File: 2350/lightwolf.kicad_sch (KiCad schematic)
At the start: 52 parts, among them Q1 XC6220B331MR-G, U1 DS1021-1X20SF11-B, U2 W25Q32JVSNIQ, U3 DS1021-1X20SF11-B, U4 RP2350A_C42411118, U5 ABM8-272-T3_C20625731, U6 0603L100SLYR

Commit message: feat: update design files and add production files
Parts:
- C12: renamed from C3; value 4.7uF -> 10uF; symbol PCM_JLCPCB-Capacitors:0402,4.7uF -> PCM_JLCPCB-Capacitors:0402,10uF; Capacitance 4.7uF -> 10uF; LCSC C23733 -> C15525; Part CL05A475MP5NRNC -> CL05A106MQ5NUNC; Price 0.008USD -> 0.009USD; Stock 3319340 -> 3940889; Voltage Rated 10V -> 6.3V
- renumbered C4 to C1, C19 to C10, C20 to C11, C9 to C13, C12 to C14, C14 to C15, C2 to C16, C5 to C17, C11 to C18, C7 to C19, C6 to C2, C8 to C3, C10 to C4, C13 to C5, C15 to C6, C16 to C7, C17 to C8, C1 to C9, H3 to H2, H2 to H3, R8 to R1, R11 to R10, R12 to R11, R13 to R12, R4 to R13, R10 to R4, R9 to R5, R5 to R6, R6 to R7, R1 to R8, R7 to R9, U5 to U1, U6 to U2, U2 to U3, U1 to U5, U3 to U6

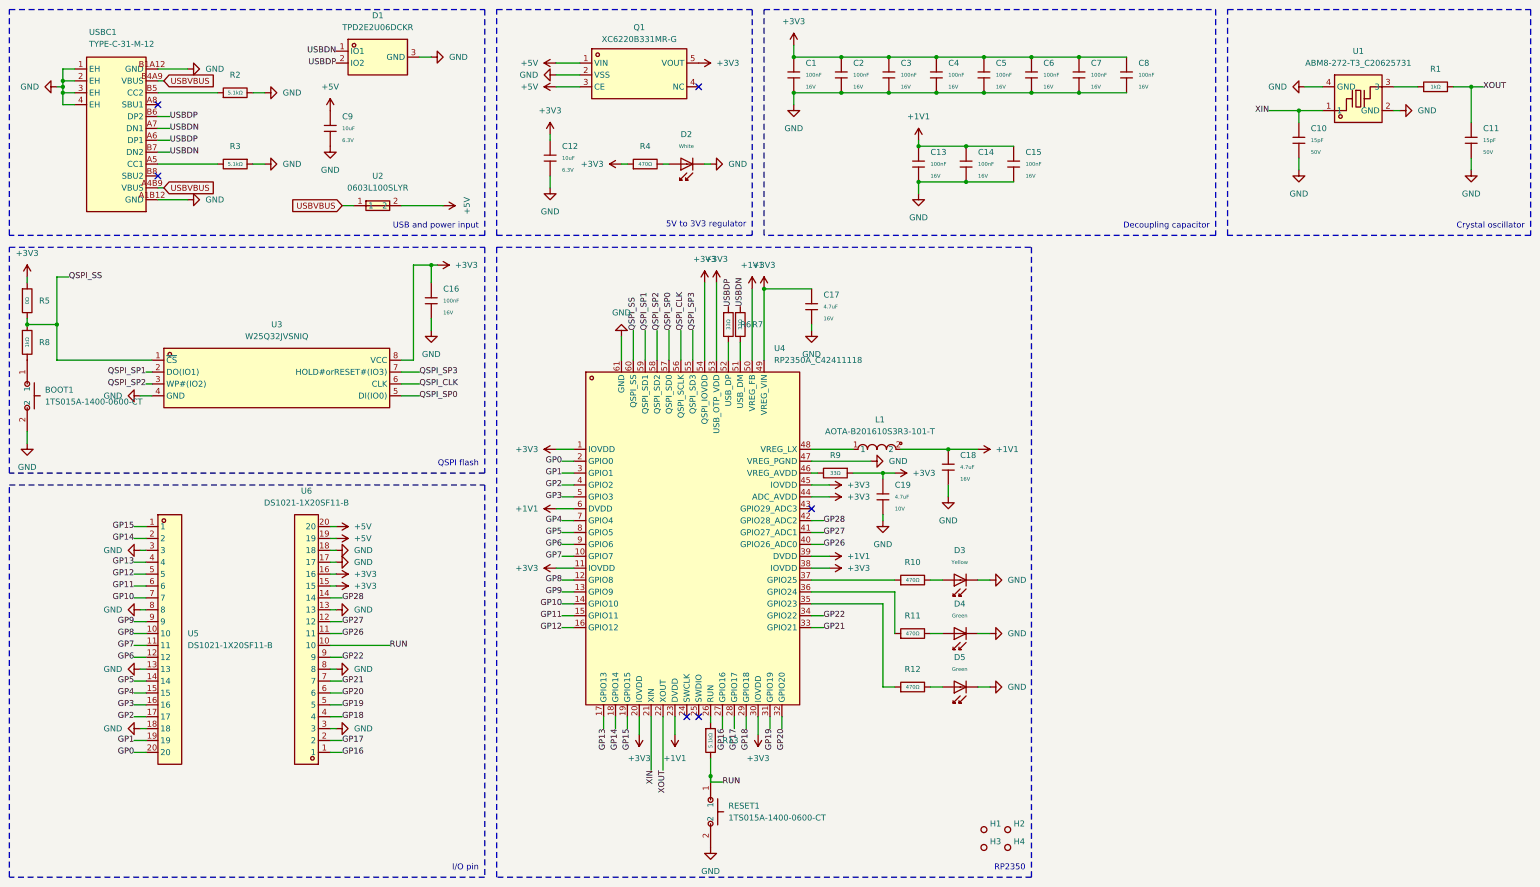
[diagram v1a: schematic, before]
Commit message: fix: design issue and update project files
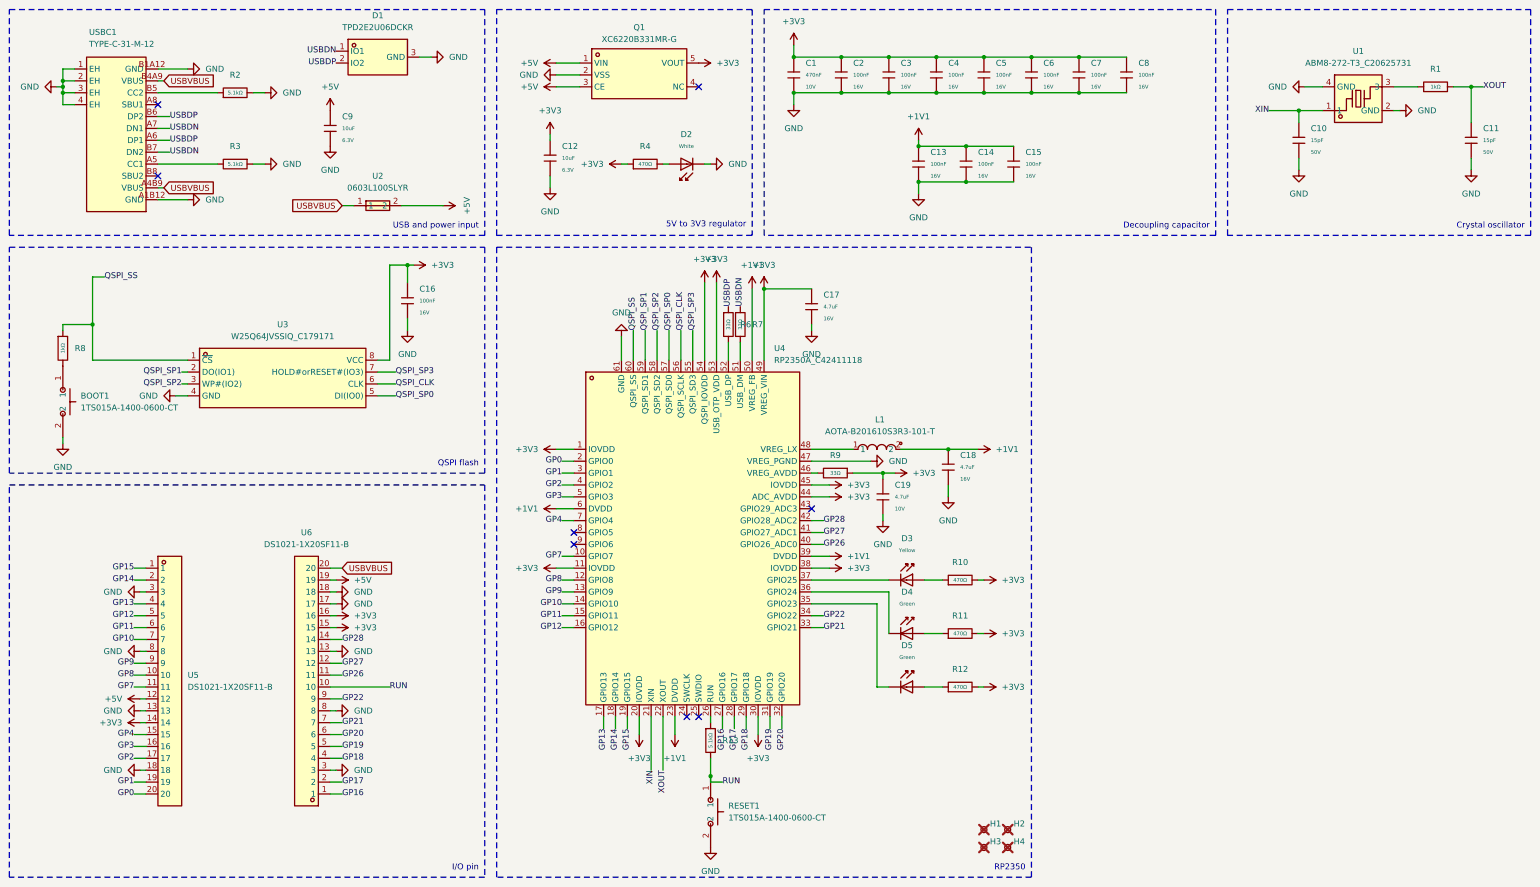
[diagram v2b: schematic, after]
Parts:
- removed D2: White, PCM_JLCPCB:D_0805, symbol PCM_JLCPCB-Diodes:LED,0805,White
- removed R5: 0Ω, PCM_JLCPCB:R_0402, symbol PCM_JLCPCB-Resistors:0402,0Ω
- added D2: White, PCM_JLCPCB:D_0603, symbol PCM_JLCPCB-Diodes:LED,0603,White
- C1: value 100nF -> 470nF; symbol PCM_JLCPCB-Capacitors:0402,100nF -> PCM_JLCPCB-Capacitors:0402,470nF; Attrition Qty 10 -> 12; Capacitance 100nF -> 470nF; Class Basic Component -> Preferred Component; LCSC C1525 -> C47339; Part CL05B104KO5NNNC -> CL05A474KP5NNNC; Price 0.004USD -> 0.007USD; Stock 14407666 -> 84633; Temperature Coefficient X7R -> X5R; Voltage Rated 16V -> 10V
- H1, H2, H3, H4: now not fitted; now left out of the parts list
- U3: value W25Q32JVSNIQ -> W25Q64JVSSIQ_C179171; footprint easyeda2kicad:SOP-8_L4.9-W3.9-P1.27-LS6.0-BL -> easyeda2kicad:SOIC-8_L5.3-W5.3-P1.27-LS8.0-BL; symbol easyeda2kicad:W25Q32JVSNIQ -> easyeda2kicad:W25Q64JVSSIQ_C179171; LCSC Part C5355146 -> C179171
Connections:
- net +3V3: now also R10.2, R11.2, R12.2, U5.14
- net +5V: now also U5.12; no longer U6.20
- net GND: now also D2.1; no longer D3.1, D4.1, D5.1
- net USBVBUS: now also U6.20
- net at R11.1: now also D4.2; no longer U4.36 (GPIO24)
- net at R12.1: now also D5.2; no longer U4.35 (GPIO23)
- net at U4.37 (GPIO25): now also D3.1; no longer R10.1
- net at D3.2: now also R10.1; no longer R10.2
- net at R4.2: now also D2.2
- net GP5: no longer names the net of U4.8 (GPIO5)
- net GP5: no longer U5.14
- net GP6: no longer names the net of U4.9 (GPIO6)
- net GP6: no longer U5.12
- new net: D5.1, U4.35 (GPIO23)
- new net: D4.1, U4.36 (GPIO24)
- no-connect marks 6 -> 8
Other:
- moved on the sheet: BOOT1, C16, D3, D4, D5, R10, R11, R12, R8, U3, U5, U6

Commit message: fix: decoupling issue for VREG_AVDD
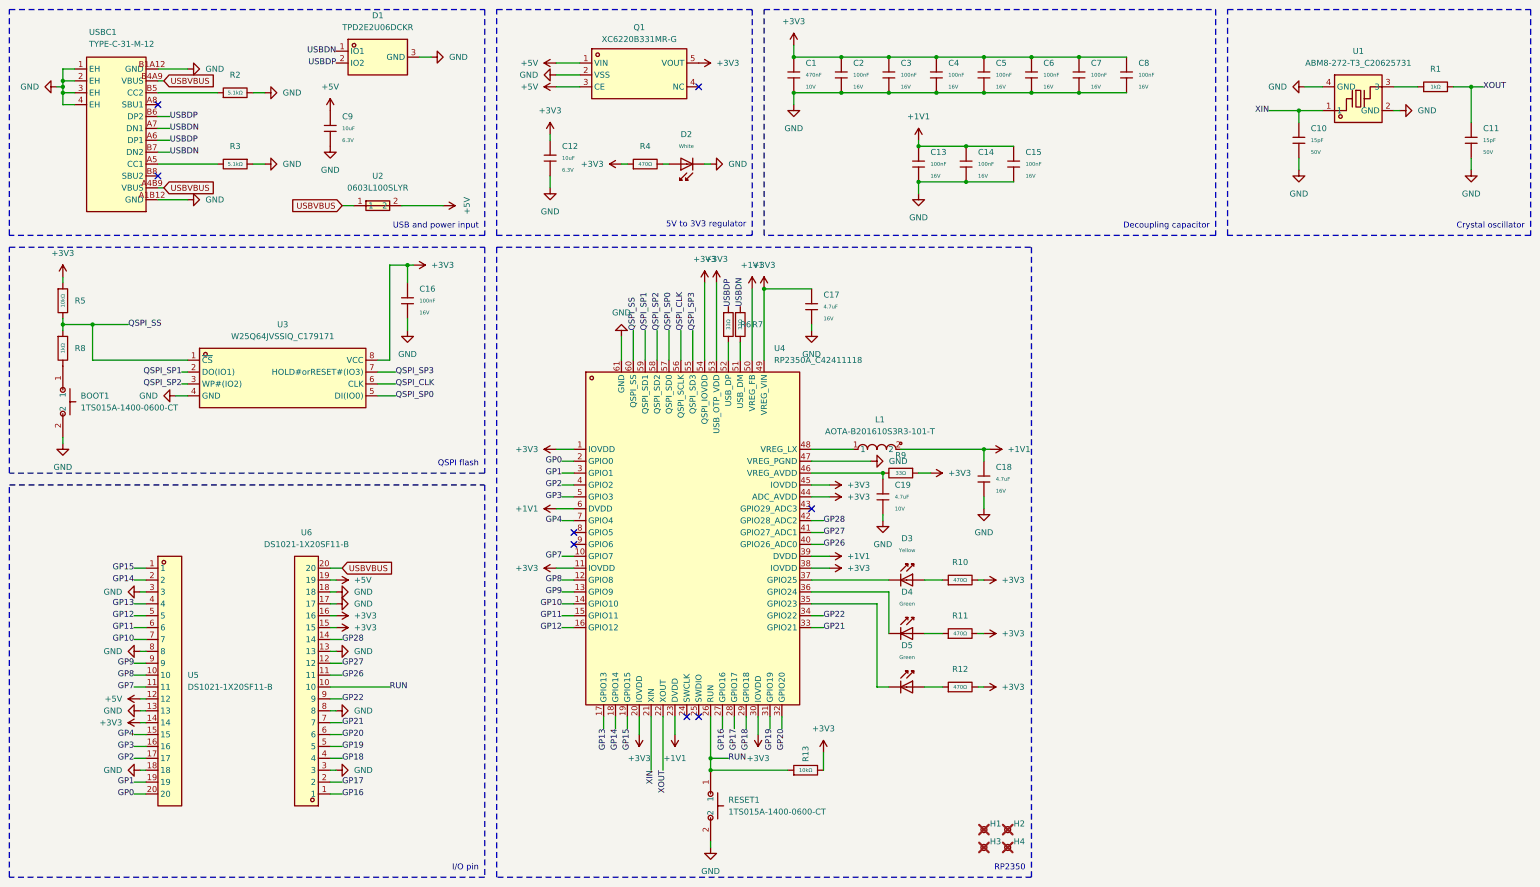
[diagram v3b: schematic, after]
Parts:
- added R5: 10kΩ, PCM_JLCPCB:R_0402, symbol PCM_JLCPCB-Resistors:0402,10kΩ
- R13: value 5.1kΩ -> 10kΩ; symbol PCM_JLCPCB-Resistors:0402,5.1kΩ -> PCM_JLCPCB-Resistors:0402,10kΩ; LCSC C25905 -> C25744; Part 0402WGF5101TCE -> 0402WGF1002TCE; Resistance 5.1kΩ -> 10kΩ; Stock 3526518 -> 24372091
- U5, U6: now left out of the parts list
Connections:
- net +3V3: now also R13.2, R5.1; no longer C19.1
- net QSPI_SS: now also R5.2
- net RUN: now also R13.1, U4.26 (RUN); no longer R13.2
- net at R9.2, U4.46 (VREG_AVDD): now also C19.1
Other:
- moved on the sheet: C18, R13, R9, RESET1
